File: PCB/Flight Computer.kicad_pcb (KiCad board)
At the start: 6 copper layers, 30 x 60 mm, 115 parts, among them J401 Conn_01x05_Pin, J402 USB_C_Receptacle_USB2.0_16P, J403 Conn_01x06_Pin, J404 Screw_Terminal_01x06, J405 Screw_Terminal_01x04, J406 Conn_02x04_Counter_Clockwise, J407 Conn_02x03_Counter_Clockwise, J408 Conn_01x04, J501 Conn_Coaxial, Q101 FDN306P, Q401 SL2302S, Q601 SL2302S, Q602 SL2302S, Q603 SL2302S, SW401 SW_Push, SW402 SW_Push, U101 LM1117MP-3.3, U201 STM32F446RETx, U202 W25Q128JVS, U301 SAM-M8Q, U302 LSM6DSV320, U303 MMC5633NJL, U304 MS5607-02BA, U501 SX1262IMLTRT, U502 SKY13453-385LF, Y201 Resonator, Y501 32 MHz

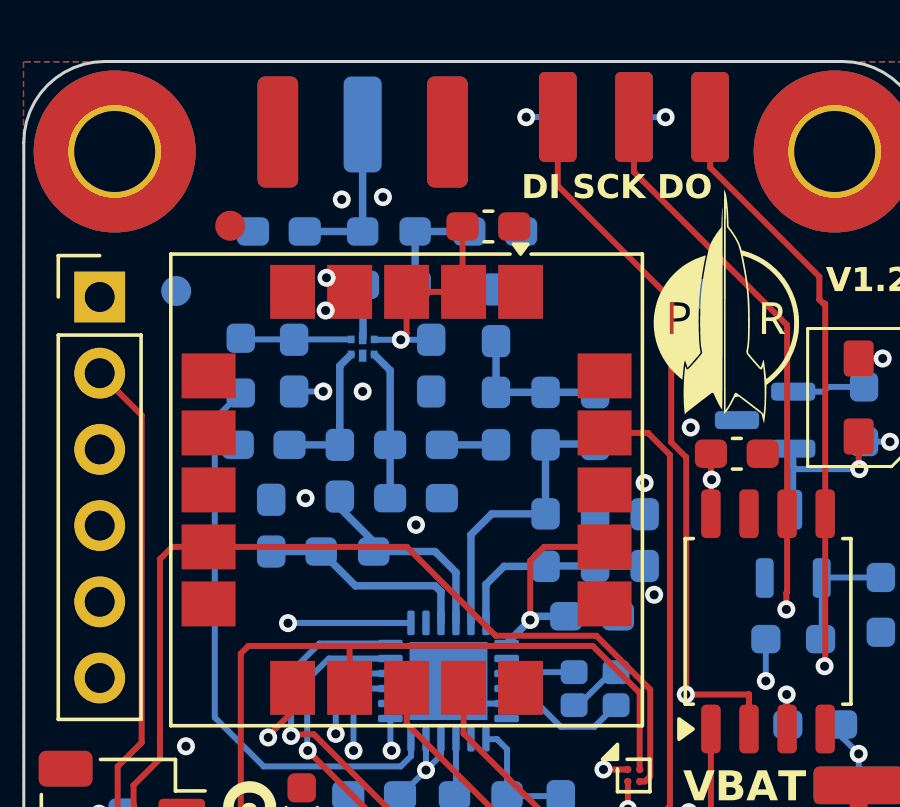
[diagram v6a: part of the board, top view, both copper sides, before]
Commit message: - Added missing inductor to make it work with 915 Mhz - Added digikey part number as a property - Reran jobset - Removed out of date BOM.xlsx - Attempted to use the config addon (didn't fully work)
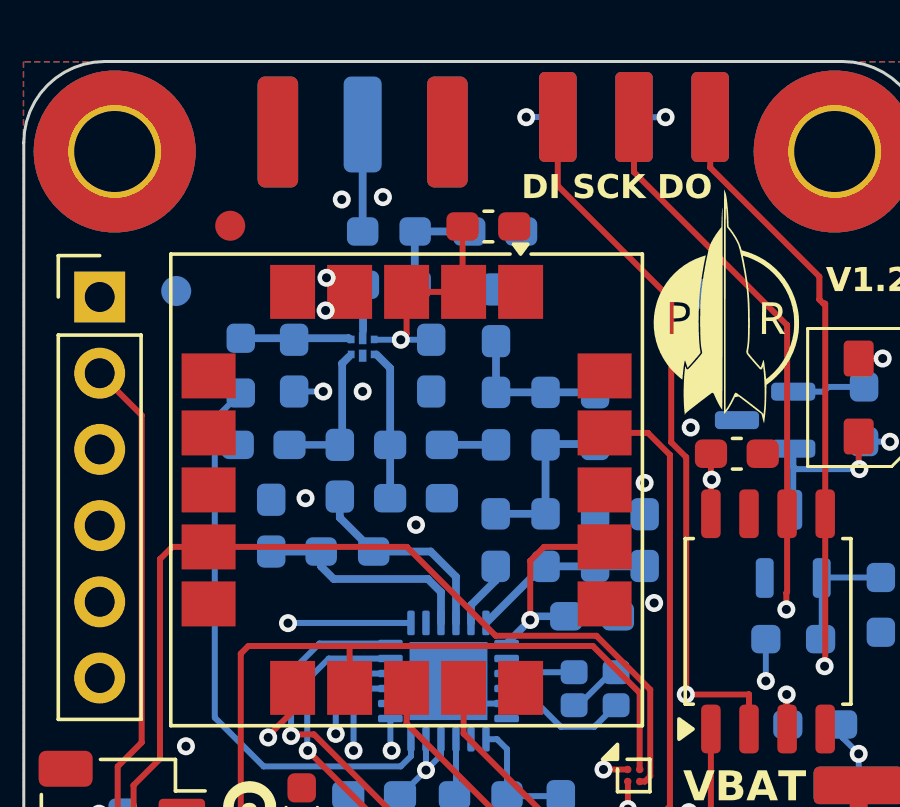
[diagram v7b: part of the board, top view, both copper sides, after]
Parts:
- removed C518: TBD, Capacitor_SMD:C_0603_1608Metric_Pad1.08x0.95mm_HandSolder
- added L507: 0R, Inductor_SMD:L_0603_1608Metric_Pad1.05x0.95mm_HandSolder, B.Cu at (113.4, 68.5)
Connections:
- C510 pad 1: /Radio/RFO_0 -> /Radio/RFO_1
- C510 pad 2: /Radio/RFO_1 -> /Radio/RFO_2
- C511 pad 1: /Radio/RFO_1 -> /Radio/RFO_2
- C512 pad 1: /Radio/RFO_3 -> /Radio/RFO_4
- C512 pad 2: /Radio/RFO_2 -> /Radio/RFO_3
- C513 pad 1: /Radio/RFO_3 -> /Radio/RFO_4
- L502 pad 2: /Radio/RFO_0 -> /Radio/RFO_1
- L504 pad 1: /Radio/RFO_0 -> /Radio/RFO_1
- L504 pad 2: /Radio/RFO_1 -> /Radio/RFO_2
- L505 pad 1: /Radio/RFO_2 -> /Radio/RFO_3
- L505 pad 2: /Radio/RFO_1 -> /Radio/RFO_2
- U502 pad 2: /Radio/RFO_3 -> /Radio/RFO_4
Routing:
- net /Radio/RFO_0: track 9.68 -> 2.23 mm
- net /Radio/RFO_4: track 0.00 -> 4.98 mm
- net /Radio/RFO_2: track 1.95 -> 5.29 mm
- net /Radio/RFO_3: track 5.01 -> 1.80 mm
- net /Radio/RF_2: track 5.50 -> 3.57 mm
- net /Radio/VR_PA: track 6.83 -> 6.09 mm
- net /Radio/RFI_N: track 7.01 -> 7.63 mm
- net /Radio/RFO_1: track 5.01 -> 5.62 mm

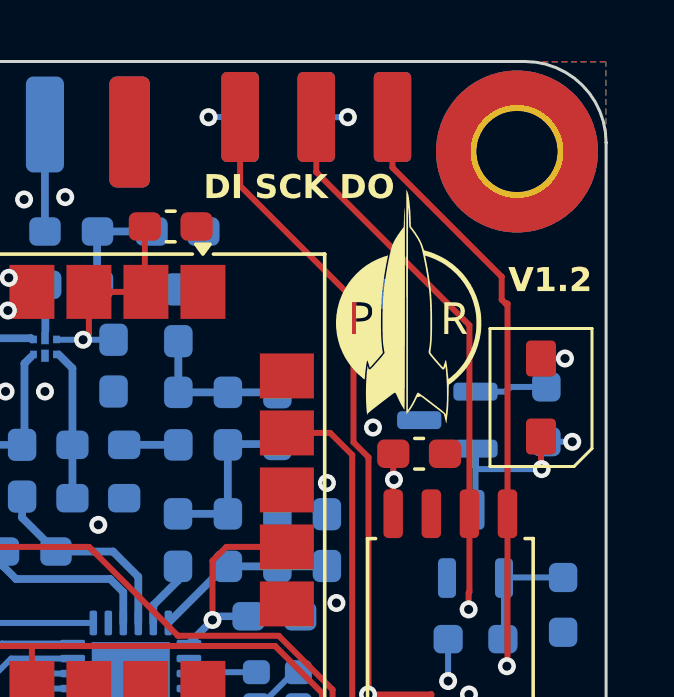
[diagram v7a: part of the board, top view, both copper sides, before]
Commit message: - Got the extension KiVar working to switch between a 433MHz and 915MHz radio - Added Digikey-PN's for the 915 MHz radio
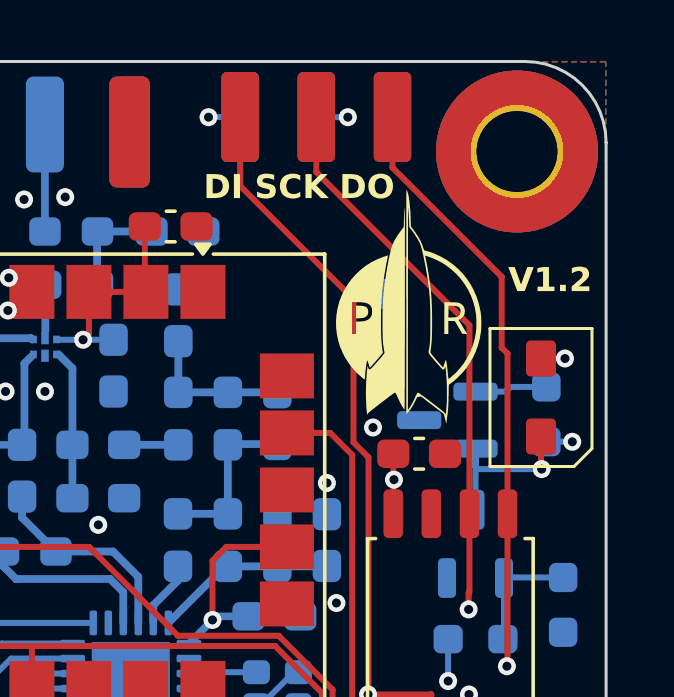
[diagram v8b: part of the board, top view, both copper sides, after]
